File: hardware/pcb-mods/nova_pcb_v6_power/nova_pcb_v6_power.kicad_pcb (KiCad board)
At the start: 4 copper layers, 112 x 90 mm, 47 parts, among them J1 XT60_4S_IN, J12 XT30_JET_12V, J13 XT30_L2_12V, J2 UBEC_5V_AUX, J20 IB_2x06, J3 XT30_Inj, J4 XT30_Inj, J5 XT30_Inj, J6 XT30_Inj, J7 XT30_Inj, J8 ServoBus_TTL, M1 Voltmeter_DC, Q1 IRLB3034PBF, Q2 BSS138_cutoff, SW1 Rocker_30A, SW2 Estop_NC_latching, U1 Pololu_D42V110F7_LEG_7V5, U10 INA226, U11 INA226, U2 Pololu_D42V110F12_HIP_12V, U3 Pololu_D24V22F12_L2_12V, U4 Pololu_D42V55F12_JET_12V, U5 Pololu_D42V55F7_ARM_7V5, U8 LM393, U9 INA226

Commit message: pcb(v6-power): route power rails + add HighCurrent/Power netclasses
Headless-route all power-appropriate rails: RAW buck->INA hops, V12_JET and
V12_L2 output rails, V7V5_LEG F.Cu pour + J6 tap, V12_HIP INA->C5, and
V12_L2_RAW buck->inductor. DRC clean (0 errors); 50 ratsnest links remain,
all GUI-bound (bottom-right logic cluster + 5 power/edge taps boxed behind
existing B.Cu walls / top THT congestion).

Add HighCurrent (3.0mm track) and Power (1.5mm) netclasses to .kicad_pro and
assign the leg/hip rails to HighCurrent. Per IPC-2221 at 2oz outer copper,
1.5mm carries ~7A @20C rise; hip rail (~9A) and leg trunk exceed that, so
they need >=3.0mm on any GUI reroute/re-pour. Netclasses govern new copper
only -- existing 1.5mm rail traces flagged for manual widening.

ROUTING_HANDOFF.md captures the remaining GUI punch-list with exact pad
coordinates, widen list, and route order.

Co-Authored-By: Claude Opus 4.7 <noreply@anthropic.com>
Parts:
- added C7: 100nF, Capacitor_SMD:C_0603_1608Metric, B.Cu at (124.5, 127.0)
- added R13: 10k, Resistor_SMD:R_0603_1608Metric, B.Cu at (136.9, 127.1)
- added R14: 470k, Resistor_SMD:R_0603_1608Metric, B.Cu at (132.9, 136.3)
- added R15: 1M, Resistor_SMD:R_0603_1608Metric, B.Cu at (127.7, 127.0)
- R10, R2: value DNP_tune -> 100k
- R11, R12: value DNP_tune -> 4.7k
- R3: value DNP_tune -> 22k
- R4: value DNP_tune -> 11.3k
- R5, R7, R8, R9: value DNP_tune -> 10k
- R6: value DNP_tune -> 12.1k
- moved R8 5.96 mm to (131.8, 127.2)
- moved R10 3.12 mm to (137.0, 136.1)
- moved R6 3.12 mm to (129.0, 136.1)
- moved R4 3.07 mm to (125.0, 136.1)
- moved R12 3.03 mm to (141.0, 136.0)
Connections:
- SW2 pad 2: EN_BUCKS -> EN_SW
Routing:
- net V12_L2: track 0.00 -> 109.4 mm
- net V12_L2_RAW: track 0.00 -> 76.4 mm
- net V12_JET: track 0.00 -> 69.0 mm
- net V7V5_LEG: track 0.00 -> 68.0 mm, vias 0 -> 1
- net V12_HIP: track 0.00 -> 61.7 mm
- net V12_HIP_RAW: track 0.00 -> 34.5 mm
- net V12_JET_RAW: track 0.00 -> 26.5 mm
- net V7V5_LEG_RAW: track 0.00 -> 24.5 mm
- net VBAT_PROTECTED: track 0.00 -> 1.85 mm, vias 0 -> 2
- net GND: vias 0 -> 7
- added copper zone on B.Cu, net GND
- added copper zone on F.Cu, net V7V5_LEG

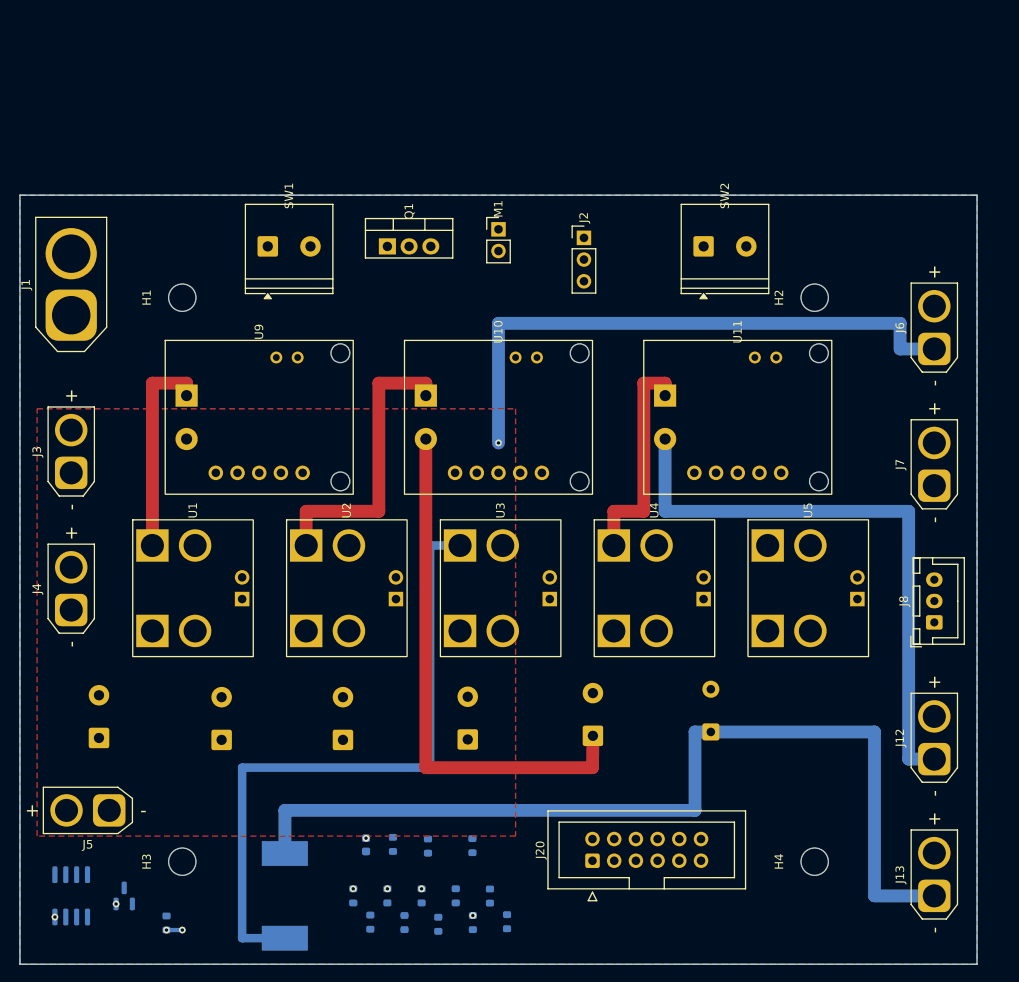
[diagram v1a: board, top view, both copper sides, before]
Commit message: pcb(v6-power-v2): fork to v2 — full reroute, safety chain, off-board INA226, DRC clean
- Fork nova_pcb_v6_power -> _v2 (v1 frozen); placement redone power-flow-first
- Safety chain board sync: Q3 e-stop inverter, Q4 EN_JET cutoff, R16, C8/C9
- INA226 modules converted off-board: footprints stripped to 4-pin I2C headers,
  RAW nets eliminated (bench wiring card in ROUTING_HANDOFF.md Step 8)
- All power routed 1.5/3.0mm per netclass, LEG pour L-shape, hip doubled F+B
- All signal nets routed headless via pre-commit collision checker:
  B.Cu lanes y137.5-139.9 + F.Cu verticals + via pairs; V5_AUX spine gap
  bridged x114.5; board min via relaxed to 0.45/0.25 (PCBWay standard)
- DRC: 0 errors, 0 unrouted; 2 zone-island seams left for GUI (Step 9)

Co-Authored-By: Claude Fable 5 <noreply@anthropic.com>
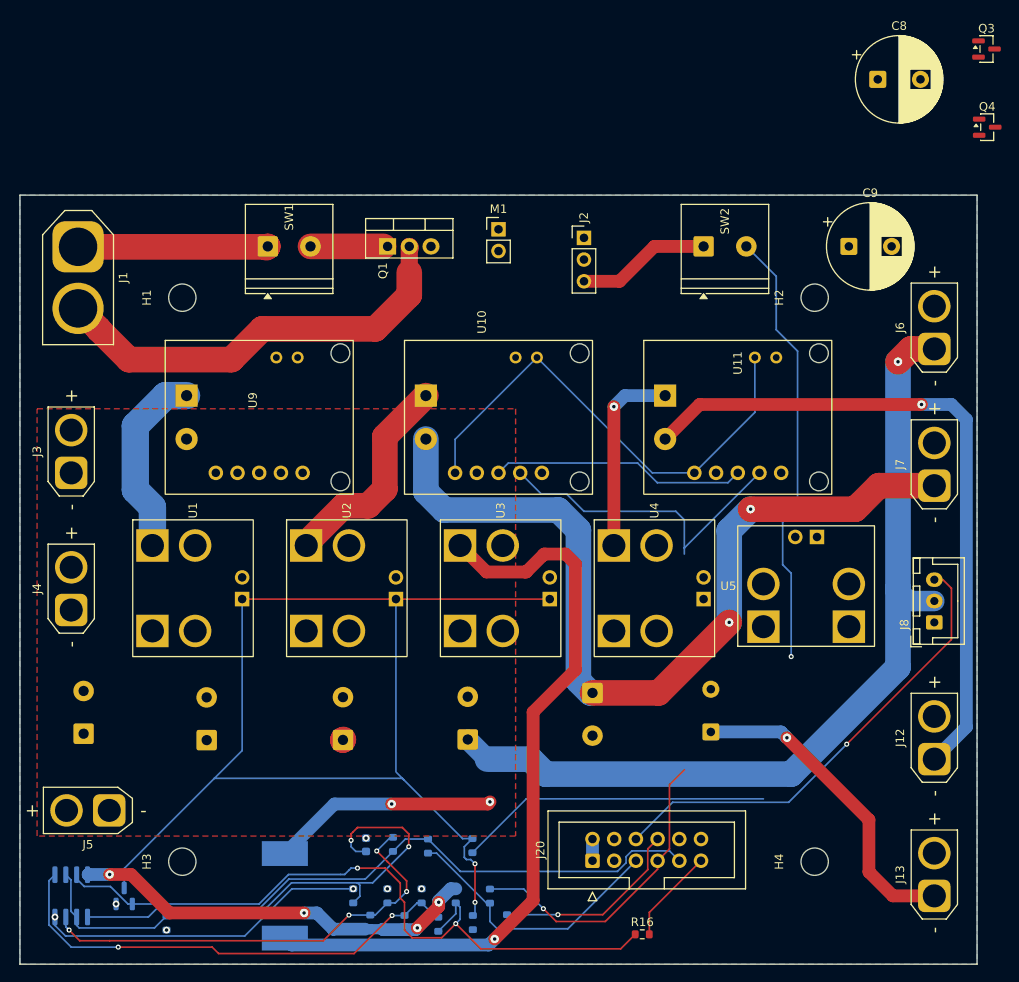
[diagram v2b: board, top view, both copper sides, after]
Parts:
- added C8: 470uF_25V, Capacitor_THT:CP_Radial_D10.0mm_P5.00mm, F.Cu at (184.4, 37.5)
- added C9: 470uF_25V, Capacitor_THT:CP_Radial_D10.0mm_P5.00mm, F.Cu at (181.0, 57.0)
- added Q3: BSS138_estop, Package_TO_SOT_SMD:SOT-23, F.Cu at (197.1, 33.9)
- added Q4: BSS138_jetcut, Package_TO_SOT_SMD:SOT-23, F.Cu at (197.2, 43.0)
- added R16: 100k, Resistor_SMD:R_0603_1608Metric, F.Cu at (156.8, 137.5)
- moved J1 8.04 mm to (90.8, 57.0), turned to -90 degrees
- moved C5 5.02 mm to (151.0, 109.2), turned to -90 degrees
- moved U5 2.83 mm to (176.0, 99.0), turned to 90 degrees
- moved C1 1.87 mm to (91.5, 114.0)
- moved C2 1.75 mm to (105.8, 114.8)
- turned R10 to -90 degrees
- turned R9 to -90 degrees
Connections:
- R13 pad 2: EN_BUCKS -> V5_AUX
- SW2 pad 1: V5_AUX -> GND
- U4 pad 3: VBAT_PROTECTED -> EN_JET
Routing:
- net EN_BUCKS: track 0.00 -> 140.3 mm, vias 0 -> 2
- net +3V3: track 0.00 -> 90.5 mm
- net EN_SW: track 0.00 -> 88.3 mm, vias 0 -> 1
- net /06 Safety Chain/HARDCUT: track 0.00 -> 85.1 mm, vias 0 -> 2
- net BATT_LOW: track 0.00 -> 76.5 mm
- net I2C_SDA: track 0.00 -> 74.6 mm, vias 0 -> 1
- net V5_AUX: track 0.00 -> 66.4 mm, vias 0 -> 4
- net /06 Safety Chain/VSENSE: track 0.00 -> 64.5 mm, vias 0 -> 2
- net /06 Safety Chain/VREF_H: track 0.00 -> 56.3 mm, vias 0 -> 2
- net BUS_SERVO: track 0.00 -> 55.0 mm, vias 0 -> 1
- net /06 Safety Chain/VREF_G: track 0.00 -> 53.2 mm, vias 0 -> 4
- net I2C_SCL: track 0.00 -> 52.6 mm, vias 0 -> 1
- net /01 Battery Input + Reverse Protection/BATT_NEG: track 0.00 -> 50.3 mm
- net GND: track 0.00 -> 49.8 mm, vias 7 -> 6
- net V12_L2: track 109.4 -> 64.2 mm, vias 0 -> 3
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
